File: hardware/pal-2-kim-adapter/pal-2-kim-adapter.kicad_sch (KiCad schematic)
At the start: 3 parts, among them J1 Peripheral, J2 KIM-1, J3 RESET

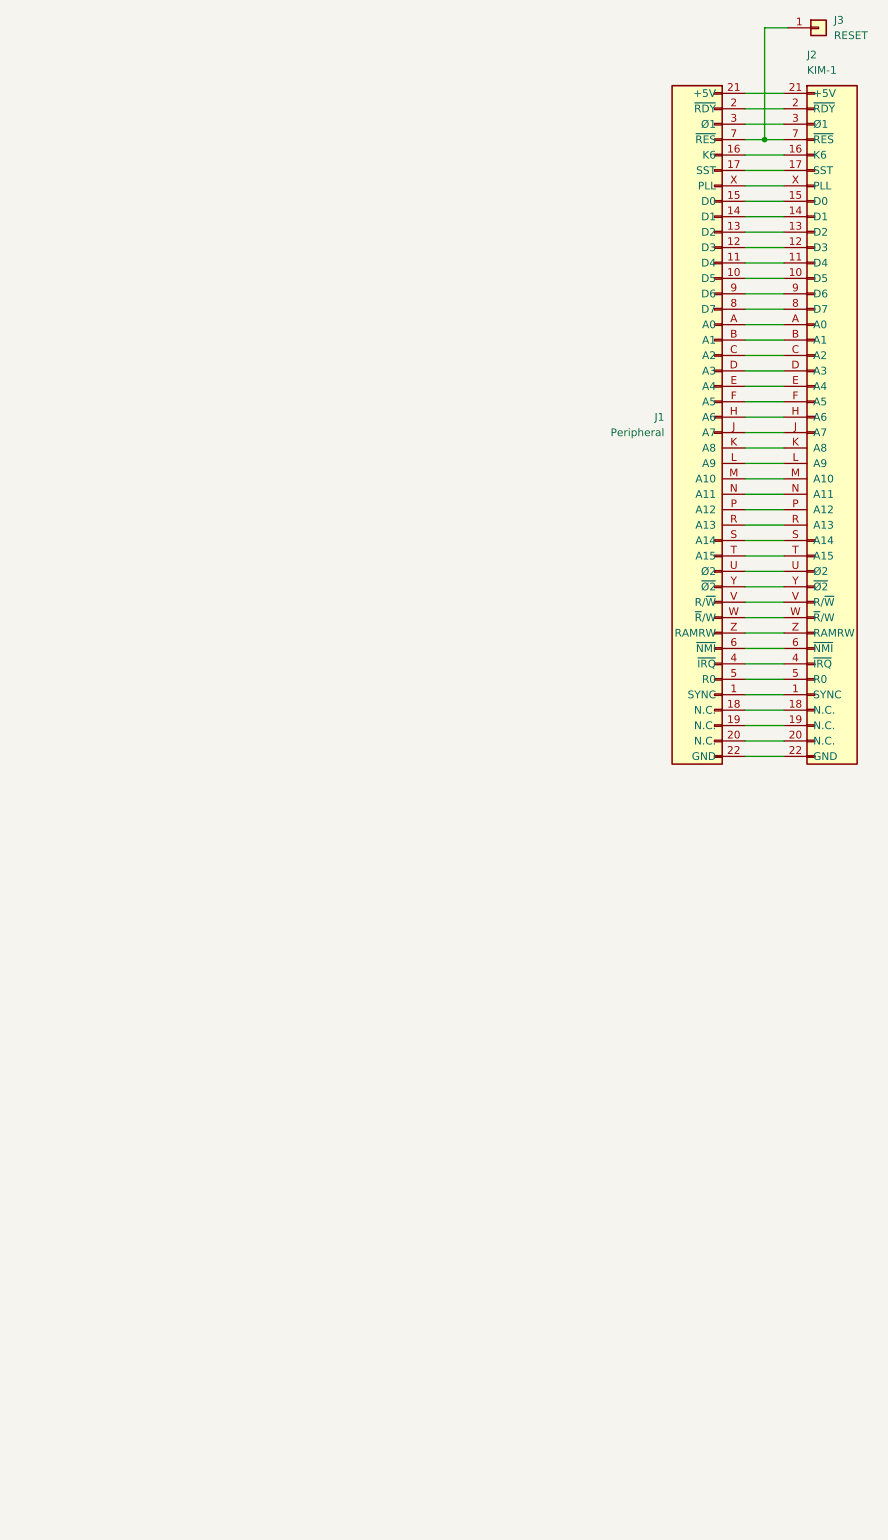
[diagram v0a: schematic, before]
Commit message: Add forced DECEN for higher addresses to the PAL-2-KIM adapter
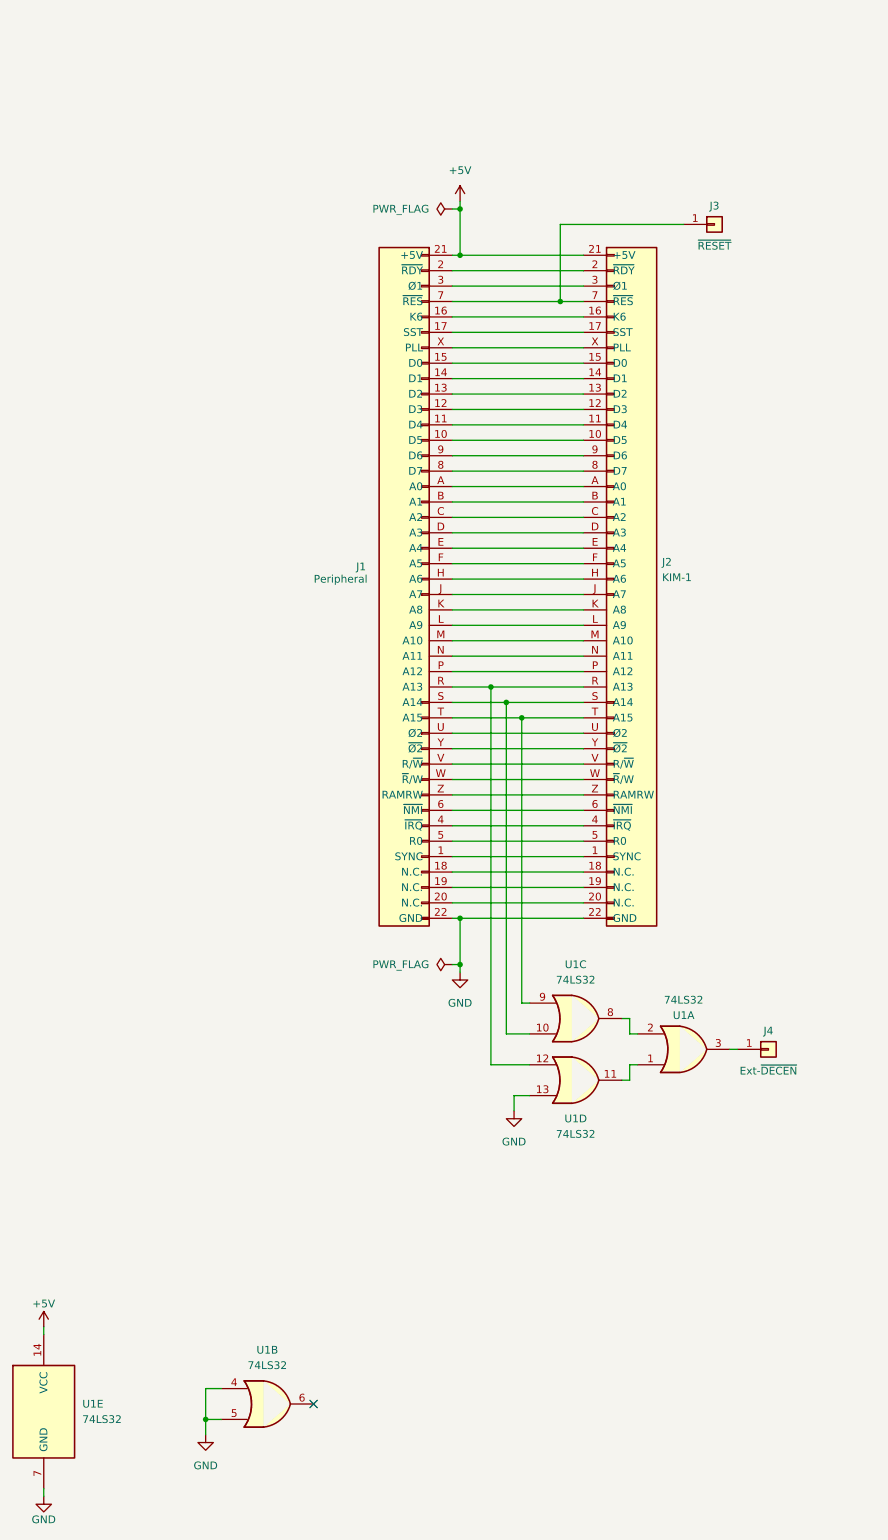
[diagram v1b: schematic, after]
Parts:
- added J4: Ext-~{DECEN}, Connector_PinHeader_2.54mm:PinHeader_1x01_P2.54mm_Vertical, symbol Connector_Generic:Conn_01x01
- added U1: 74LS32, Package_DIP:DIP-14_W7.62mm, symbol 74xx:74LS32
- J3: value RESET -> ~{RESET}
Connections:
- net +5V: now reaches J1.21 (+5V), J2.21 (+5V)
- net +5V: now also U1.14 (VCC)
- net GND: now reaches J1.22 (GND), J2.22 (GND)
- net GND: now also U1.13, U1.4, U1.5, U1.7 (GND)
- net at J1.R (A13), J2.R (A13): now also U1.12
- net at J1.S (A14), J2.S (A14): now also U1.10
- net at J1.T (A15), J2.T (A15): now also U1.9
- new net: U1.1, U1.11
- new net: J4.1 (Pin_1), U1.3
- new net: U1.2, U1.8
- no-connect marks 0 -> 1
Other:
- moved on the sheet: J2, J3
